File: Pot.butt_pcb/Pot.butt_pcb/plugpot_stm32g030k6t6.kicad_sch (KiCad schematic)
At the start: 7 parts, among them J1 Conn_01x05_Male, J2 Conn_01x06_Male, SW1 SW_Push, U1 STM32G030K6T6

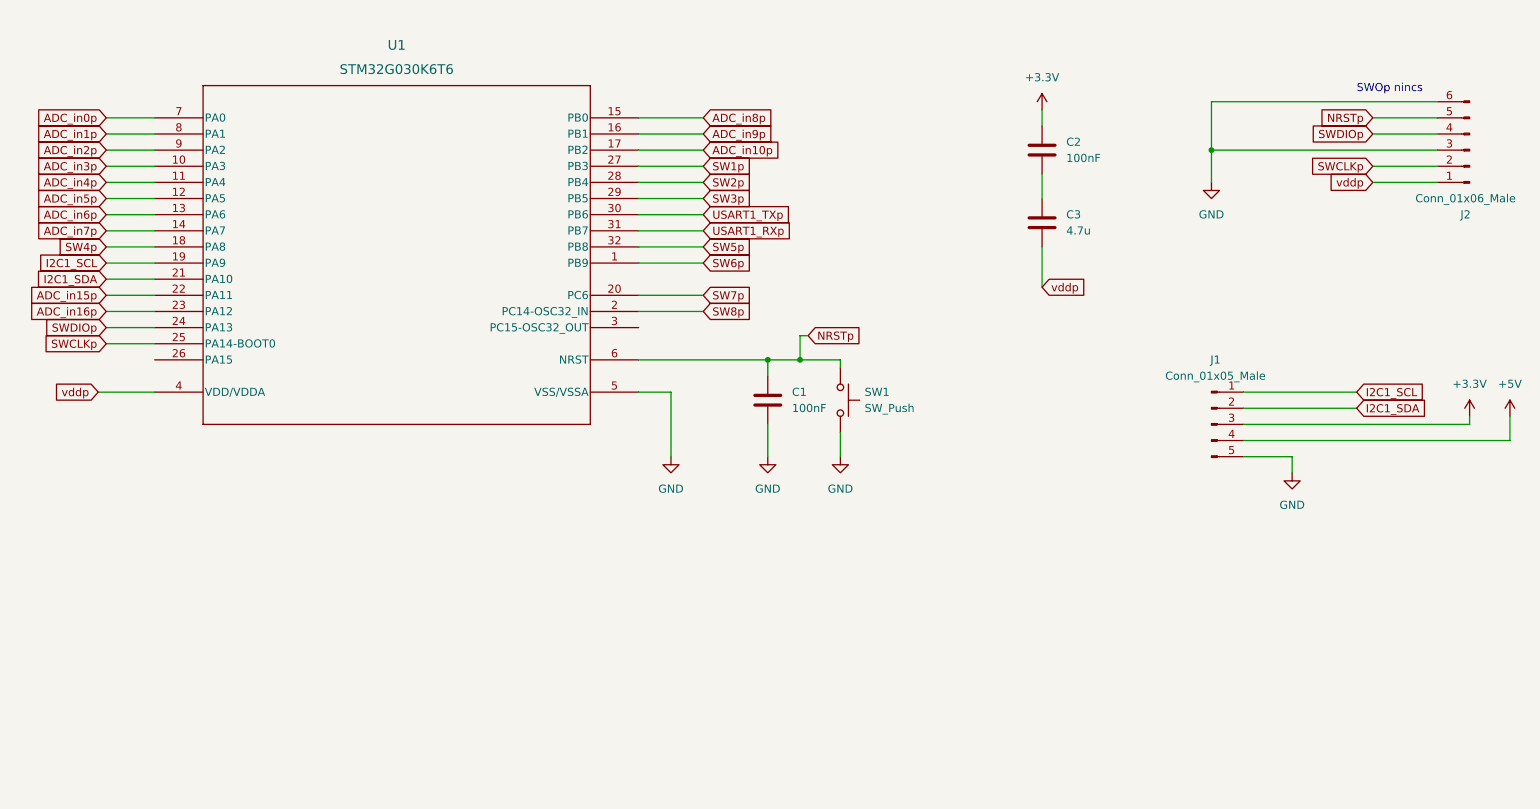
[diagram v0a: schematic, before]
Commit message: fixing keyboard and pot project schematics
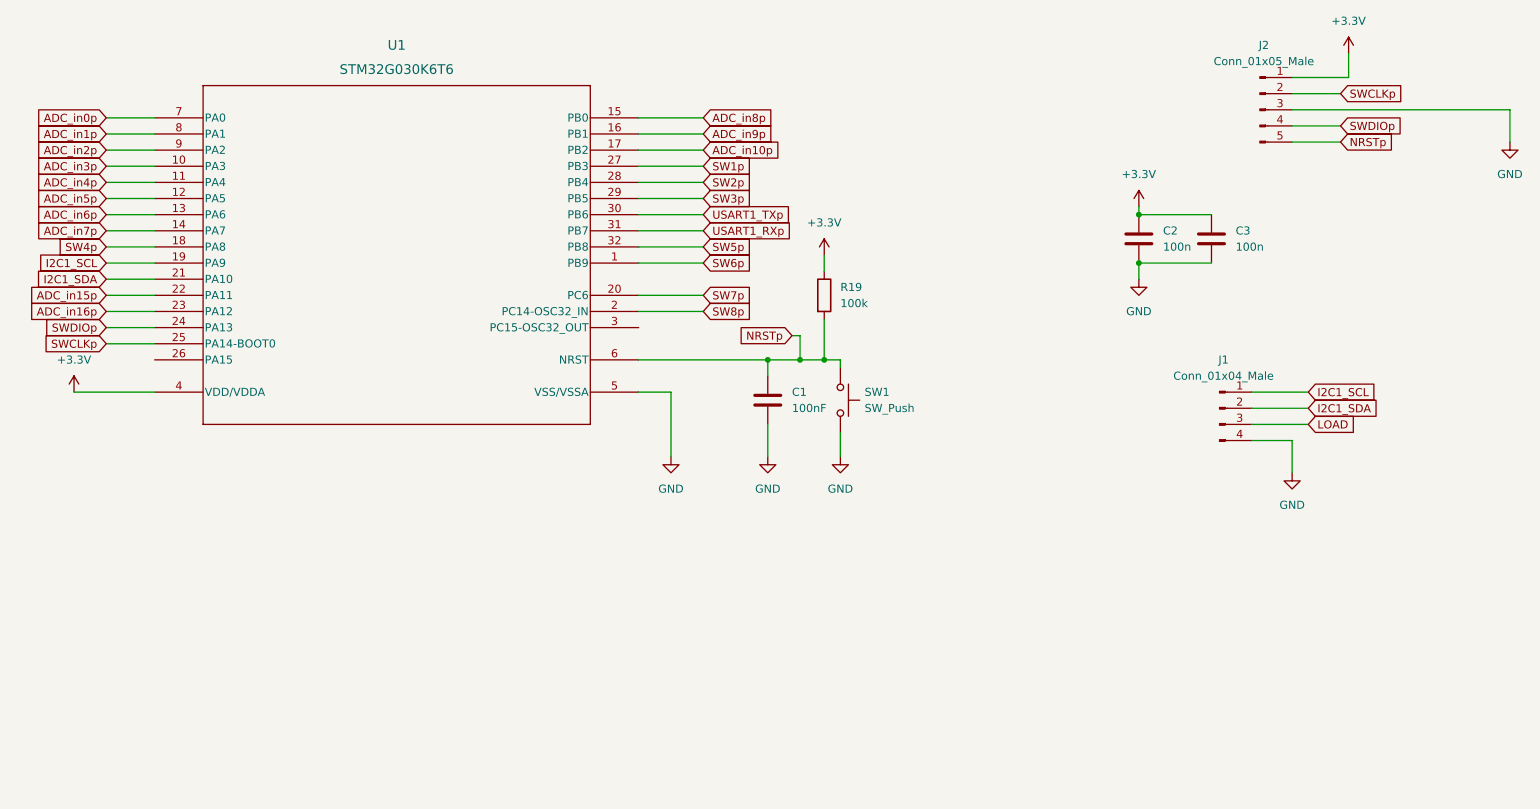
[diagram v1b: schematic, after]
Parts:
- removed J1: Conn_01x05_Male, symbol Connector:Conn_01x05_Male
- removed J2: Conn_01x06_Male, Connector_PinSocket_2.54mm:PinSocket_1x06_P2.54mm_Horizontal, symbol Connector:Conn_01x06_Male
- added J1: Conn_01x04_Male, symbol Connector:Conn_01x04_Male
- added J2: Conn_01x05_Male, symbol Connector:Conn_01x05_Male
- added R19: 100k, Resistor_SMD:R_0805_2012Metric_Pad1.20x1.40mm_HandSolder, symbol Device:R
- C2: value 100nF -> 100n
- C3: value 4.7u -> 100n
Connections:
- net +3V3: now also C3.1, U1.4 (VDD/VDDA), J2.1 (Pin_1), R19.1
- net GND: now also C2.2, C3.2, J1.4 (Pin_4), J2.3 (Pin_3)
- net I2C1_SCL: now also J1.1 (Pin_1)
- net I2C1_SDA: now also J1.2 (Pin_2)
- net NRSTp: now also J2.5 (Pin_5), R19.2
- net SWCLKp: now also J2.2 (Pin_2)
- net SWDIOp: now also J2.4 (Pin_4)
- removed net vddp: C3.2, U1.4 (VDD/VDDA)
- new net LOAD: J1.3 (Pin_3)
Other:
- note removed: "SWOp nincs"

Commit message: main_func pcb done
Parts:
- added D53: GREEN LED, LED_SMD:LED_0805_2012Metric_Pad1.15x1.40mm_HandSolder, symbol Device:LED
- added D54: RED LED, LED_SMD:LED_0805_2012Metric_Pad1.15x1.40mm_HandSolder, symbol Device:LED
- added R27, R28: 1k, Resistor_SMD:R_0805_2012Metric_Pad1.20x1.40mm_HandSolder, symbol Device:R
- C2, C3: value 100n -> 100nF
- J1: footprint (none) -> Connector_PinSocket_2.54mm:PinSocket_1x04_P2.54mm_Horizontal
- J2: footprint (none) -> Connector_PinSocket_2.54mm:PinSocket_1x05_P2.54mm_Horizontal
- SW1: footprint (none) -> tactile_button:ROCPU Switches TP10721645
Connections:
- net +3V3: now also D53.2 (A)
- net GND: now also D54.1 (K)
- net USART1_TXp: now also R27.1, R28.1
- new net: D54.2 (A), R28.2
- new net: D53.1 (K), R27.2
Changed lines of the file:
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@@
   (junction (at 147.32 88.9) (diameter 0) (color 0 0 0 0)
   )
+  (junction (at 191.3094 115.6909) (diameter 0) (color 0 0 0 0)
+  )
   (junction (at 205.74 66.04) (diameter 0) (color 0 0 0 0)
   )
@@
   (junction (at 156.21 88.9) (diameter 0) (color 0 0 0 0)
   )
+  (wire (pts (xy 173.5294 115.6909) (xy 173.5294 119.5009))
+    (stroke (width 0) (type default) (color 0 0 0 0))
+  )
   (wire (pts (xy 223.52 93.98) (xy 232.41 93.98))
     (stroke (width 0) (type default) (color 0 0 0 0))
@@
     (stroke (width 0) (type default) (color 0 0 0 0))
   )
+  (wire (pts (xy 191.3094 115.6909) (xy 191.3094 119.5009))
+    (stroke (width 0) (type default) (color 0 0 0 0))
+  )
   (wire (pts (xy 43.18 81.28) (xy 50.8 81.28))
     (stroke (width 0) (type default) (color 0 0 0 0))
@@
     (stroke (width 0) (type default) (color 0 0 0 0))
   )
+  (wire (pts (xy 173.5294 148.7109) (xy 173.5294 139.8209))
+    (stroke (width 0) (type default) (color 0 0 0 0))
+  )
   (wire (pts (xy 229.87 49.53) (xy 264.16 49.53))
     (stroke (width 0) (type default) (color 0 0 0 0))
@@
     (stroke (width 0) (type default) (color 0 0 0 0))
   )
+  (wire (pts (xy 198.9294 115.6909) (xy 191.3094 115.6909))
+    (stroke (width 0) (type default) (color 0 0 0 0))
+  )
   (wire (pts (xy 132.08 93.98) (xy 132.08 104.14))
     (stroke (width 0) (type default) (color 0 0 0 0))
@@
     (stroke (width 0) (type default) (color 0 0 0 0))
   )
+  (wire (pts (xy 191.3094 127.1209) (xy 191.3094 132.2009))
+    (stroke (width 0) (type default) (color 0 0 0 0))
+  )
   (wire (pts (xy 127 66.04) (xy 137.16 66.04))
     (stroke (width 0) (type default) (color 0 0 0 0))
@@
     (stroke (width 0) (type default) (color 0 0 0 0))
   )
+  (wire (pts (xy 168.4494 146.1709) (xy 168.4494 148.7109))
+    (stroke (width 0) (type default) (color 0 0 0 0))
+  )
+  (wire (pts (xy 191.3094 115.6909) (xy 173.5294 115.6909))
+    (stroke (width 0) (type default) (color 0 0 0 0))
+  )
   (wire (pts (xy 156.21 72.39) (xy 156.21 74.93))
     (stroke (width 0) (type default) (color 0 0 0 0))
@@
     (stroke (width 0) (type default) (color 0 0 0 0))
   )
+  (wire (pts (xy 173.5294 127.1209) (xy 173.5294 132.2009))
+    (stroke (width 0) (type default) (color 0 0 0 0))
+  )
   (wire (pts (xy 205.74 73.66) (xy 205.74 76.2))
     (stroke (width 0) (type default) (color 0 0 0 0))
   )
+  (wire (pts (xy 191.3094 139.8209) (xy 191.3094 147.4409))
+    (stroke (width 0) (type default) (color 0 0 0 0))
+  )
   (wire (pts (xy 127 73.66) (xy 137.16 73.66))
     (stroke (width 0) (type default) (color 0 0 0 0))
   )
+  (wire (pts (xy 168.4494 148.7109) (xy 173.5294 148.7109))
+    (stroke (width 0) (type default) (color 0 0 0 0))
+  )
   (wire (pts (xy 229.87 101.6) (xy 229.87 106.68))
     (stroke (width 0) (type default) (color 0 0 0 0))
@@
     (effects (font (size 1.27 1.27)) (justify left))
     (property "Intersheet References" "${INTERSHEET_REFS}" (id 0) (at 144.5926 71.0406 0)
+      (effects (font (size 1.27 1.27)) (justify left) hide)
+    )
+  )
+  (global_label "USART1_TXp" (shape input) (at 198.9294 115.6909 0) (fields_autoplaced)
+    (effects (font (size 1.27 1.27)) (justify left))
+    (property "Intersheet References" "${INTERSHEET_REFS}" (id 0) (at 212.712 115.6115 0)
       (effects (font (size 1.27 1.27)) (justify left) hide)
     )
@@
     (property "Reference" "J2" (id 0) (at 225.425 39.37 0))
     (property "Value" "Conn_01x05_Male" (id 1) (at 225.425 41.91 0))
-    (property "Footprint" "" (id 2) (at 224.79 49.53 0)
+    (property "Footprint" "Connector_PinSocket_2.54mm:PinSocket_1x05_P2.54mm_Horizontal" (id 2) (at 224.79 49.53 0)
       (effects (font (size 1.27 1.27)) hide)
     )
@@
       (effects (font (size 1.27 1.27)) (justify left))
     )
-    (property "Value" "100n" (id 1) (at 220.98 71.1199 0)
+    (property "Value" "100nF" (id 1) (at 220.98 71.1199 0)
       (effects (font (size 1.27 1.27)) (justify left))
     )
@@
     (property "Reference" "J1" (id 0) (at 219.075 88.9 0))
     (property "Value" "Conn_01x04_Male" (id 1) (at 219.075 91.44 0))
-    (property "Footprint" "" (id 2) (at 218.44 96.52 0)
+    (property "Footprint" "Connector_PinSocket_2.54mm:PinSocket_1x04_P2.54mm_Horizontal" (id 2) (at 218.44 96.52 0)
       (effects (font (size 1.27 1.27)) hide)
     )
@@
     (pin "1")
   )
+  (symbol (lib_id "power:+3.3V") (at 168.4494 146.1709 0) (unit 1)
+    (in_bom yes) (on_board yes) (fields_autoplaced)
+    (property "Reference" "#PWR022" (id 0) (at 168.4494 149.9809 0)
+      (effects (font (size 1.27 1.27)) hide)
+    )
+    (property "Value" "+3.3V" (id 1) (at 168.4494 141.0909 0))
+    (property "Footprint" "" (id 2) (at 168.4494 146.1709 0)
+      (effects (font (size 1.27 1.27)) hide)
+    )
+    (property "Datasheet" "" (id 3) (at 168.4494 146.1709 0)
+      (effects (font (size 1.27 1.27)) hide)
+    )
+    (pin "1")
+  )
   (symbol (lib_id "power:+3.3V") (at 205.74 64.77 0) (unit 1)
     (in_bom yes) (on_board yes) (fields_autoplaced)
@@
       (effects (font (size 1.27 1.27)) (justify left))
     )
-    (property "Footprint" "" (id 2) (at 163.83 95.25 0)
+    (property "Footprint" "tactile_button:ROCPU Switches TP10721645" (id 2) (at 163.83 95.25 0)
       (effects (font (size 1.27 1.27)) hide)
     )
     (property "Datasheet" "~" (id 3) (at 163.83 95.25 0)
+      (effects (font (size 1.27 1.27)) hide)
+    )
+    (pin "1")
+    (pin "2")
+  )
+  (symbol (lib_id "Device:R") (at 191.3094 123.3109 0) (unit 1)
+    (in_bom yes) (on_board yes) (fields_autoplaced)
+    (property "Reference" "R28" (id 0) (at 193.8494 122.0408 0)
+      (effects (font (size 1.27 1.27)) (justify left))
+    )
+    (property "Value" "1k" (id 1) (at 193.8494 124.5808 0)
+      (effects (font (size 1.27 1.27)) (justify left))
+    )
+    (property "Footprint" "Resistor_SMD:R_0805_2012Metric_Pad1.20x1.40mm_HandSolder" (id 2) (at 189.5314 123.3109 90)
+      (effects (font (size 1.27 1.27)) hide)
+    )
+    (property "Datasheet" "~" (id 3) (at 191.3094 123.3109 0)
       (effects (font (size 1.27 1.27)) hide)
     )
@@
     (pin "9")
   )
+  (symbol (lib_id "power:GND") (at 191.3094 147.4409 0) (unit 1)
+    (in_bom yes) (on_board yes) (fields_autoplaced)
+    (property "Reference" "#PWR023" (id 0) (at 191.3094 153.7909 0)
+      (effects (font (size 1.27 1.27)) hide)
+    )
+    (property "Value" "GND" (id 1) (at 191.3094 152.5209 0))
+    (property "Footprint" "" (id 2) (at 191.3094 147.4409 0)
+      (effects (font (size 1.27 1.27)) hide)
+    )
+    (property "Datasheet" "" (id 3) (at 191.3094 147.4409 0)
+      (effects (font (size 1.27 1.27)) hide)
+    )
+    (pin "1")
+  )
   (symbol (lib_id "Device:C") (at 205.74 69.85 0) (unit 1)
     (in_bom yes) (on_board yes) (fields_autoplaced)
@@
       (effects (font (size 1.27 1.27)) (justify left))
     )
-    (property "Value" "100n" (id 1) (at 209.55 71.1199 0)
+    (property "Value" "100nF" (id 1) (at 209.55 71.1199 0)
       (effects (font (size 1.27 1.27)) (justify left))
     )
@@
     (pin "1")
   )
+  (symbol (lib_id "Device:LED") (at 191.3094 136.0109 90) (unit 1)
+    (in_bom yes) (on_board yes) (fields_autoplaced)
+    (property "Reference" "D54" (id 0) (at 195.1194 136.3283 90)
+      (effects (font (size 1.27 1.27)) (justify right))
+    )
+    (property "Value" "RED LED" (id 1) (at 195.1194 138.8683 90)
+      (effects (font (size 1.27 1.27)) (justify right))
+    )
+    (property "Footprint" "LED_SMD:LED_0805_2012Metric_Pad1.15x1.40mm_HandSolder" (id 2) (at 191.3094 136.0109 0)
+      (effects (font (size 1.27 1.27)) hide)
+    )
+    (property "Datasheet" "~" (id 3) (at 191.3094 136.0109 0)
+      (effects (font (size 1.27 1.27)) hide)
+    )
+    (pin "1")
+    (pin "2")
+  )
   (symbol (lib_id "power:GND") (at 132.08 104.14 0) (unit 1)
     (in_bom yes) (on_board yes) (fields_autoplaced)
@@
     (pin "1")
   )
+  (symbol (lib_id "Device:R") (at 173.5294 123.3109 0) (unit 1)
+    (in_bom yes) (on_board yes) (fields_autoplaced)
+    (property "Reference" "R27" (id 0) (at 176.0694 122.0408 0)
+      (effects (font (size 1.27 1.27)) (justify left))
+    )
+    (property "Value" "1k" (id 1) (at 176.0694 124.5808 0)
+      (effects (font (size 1.27 1.27)) (justify left))
+    )
+    (property "Footprint" "Resistor_SMD:R_0805_2012Metric_Pad1.20x1.40mm_HandSolder" (id 2) (at 171.7514 123.3109 90)
+      (effects (font (size 1.27 1.27)) hide)
+    )
+    (property "Datasheet" "~" (id 3) (at 173.5294 123.3109 0)
+      (effects (font (size 1.27 1.27)) hide)
+    )
+    (pin "1")
+    (pin "2")
+  )
+  (symbol (lib_id "Device:LED") (at 173.5294 136.0109 270) (unit 1)
+    (in_bom yes) (on_board yes) (fields_autoplaced)
+    (property "Reference" "D53" (id 0) (at 176.0694 133.1533 90)
+      (effects (font (size 1.27 1.27)) (justify left))
+    )
+    (property "Value" "GREEN LED" (id 1) (at 176.0694 135.6933 90)
+      (effects (font (size 1.27 1.27)) (justify left))
+    )
+    (property "Footprint" "LED_SMD:LED_0805_2012Metric_Pad1.15x1.40mm_HandSolder" (id 2) (at 173.5294 136.0109 0)
+      (effects (font (size 1.27 1.27)) hide)
+    )
+    (property "Datasheet" "~" (id 3) (at 173.5294 136.0109 0)
+      (effects (font (size 1.27 1.27)) hide)
+    )
+    (pin "1")
+    (pin "2")
+  )
 )

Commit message: Pot.but_pcb in progress
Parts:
- J1: footprint Connector_PinSocket_2.54mm:PinSocket_1x04_P2.54mm_Horizontal -> Connector_PinSocket_2.54mm:PinSocket_1x04_P2.54mm_Vertical
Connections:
- net SW1p: now also U1.18 (PA8); no longer U1.27 (PB3)
- net SW2p: now also U1.20 (PC6); no longer U1.28 (PB4)
- net SW3p: now also U1.27 (PB3); no longer U1.29 (PB5)
- net SW4p: now also U1.28 (PB4); no longer U1.18 (PA8)
- net SW5p: now also U1.29 (PB5); no longer U1.32 (PB8)
- net SW6p: now also U1.32 (PB8); no longer U1.1 (PB9)
- net SW7p: now also U1.2 (PC14-OSC32_IN); no longer U1.20 (PC6)
- net SW8p: now also U1.1 (PB9); no longer U1.2 (PC14-OSC32_IN)
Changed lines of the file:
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@@
     )
   )
-  (global_label "SW2p" (shape input) (at 137.16 60.96 0) (fields_autoplaced)
+  (global_label "SW4p" (shape input) (at 137.16 60.96 0) (fields_autoplaced)
     (effects (font (size 1.27 1.27)) (justify left))
     (property "Intersheet References" "${INTERSHEET_REFS}" (id 0) (at 144.5926 60.8806 0)
@@
     )
   )
-  (global_label "SW3p" (shape input) (at 137.16 63.5 0) (fields_autoplaced)
+  (global_label "SW5p" (shape input) (at 137.16 63.5 0) (fields_autoplaced)
     (effects (font (size 1.27 1.27)) (justify left))
     (property "Intersheet References" "${INTERSHEET_REFS}" (id 0) (at 144.5926 63.4206 0)
@@
     )
   )
-  (global_label "SW5p" (shape input) (at 137.16 71.12 0) (fields_autoplaced)
+  (global_label "SW6p" (shape input) (at 137.16 71.12 0) (fields_autoplaced)
     (effects (font (size 1.27 1.27)) (justify left))
     (property "Intersheet References" "${INTERSHEET_REFS}" (id 0) (at 144.5926 71.0406 0)
@@
     )
   )
-  (global_label "SW1p" (shape input) (at 137.16 58.42 0) (fields_autoplaced)
+  (global_label "SW3p" (shape input) (at 137.16 58.42 0) (fields_autoplaced)
     (effects (font (size 1.27 1.27)) (justify left))
     (property "Intersheet References" "${INTERSHEET_REFS}" (id 0) (at 144.5926 58.3406 0)
@@
     )
   )
-  (global_label "SW4p" (shape input) (at 43.18 71.12 180) (fields_autoplaced)
+  (global_label "SW1p" (shape input) (at 43.18 71.12 180) (fields_autoplaced)
     (effects (font (size 1.27 1.27)) (justify right))
     (property "Intersheet References" "${INTERSHEET_REFS}" (id 0) (at 35.7474 71.0406 0)
@@
     )
   )
-  (global_label "SW8p" (shape input) (at 137.16 81.28 0) (fields_autoplaced)
+  (global_label "SW7p" (shape input) (at 137.16 81.28 0) (fields_autoplaced)
     (effects (font (size 1.27 1.27)) (justify left))
     (property "Intersheet References" "${INTERSHEET_REFS}" (id 0) (at 144.5926 81.2006 0)
@@
     )
   )
-  (global_label "SW7p" (shape input) (at 137.16 78.74 0) (fields_autoplaced)
+  (global_label "SW2p" (shape input) (at 137.16 78.74 0) (fields_autoplaced)
     (effects (font (size 1.27 1.27)) (justify left))
     (property "Intersheet References" "${INTERSHEET_REFS}" (id 0) (at 144.5926 78.6606 0)
@@
     )
   )
-  (global_label "SW6p" (shape input) (at 137.16 73.66 0) (fields_autoplaced)
+  (global_label "SW8p" (shape input) (at 137.16 73.66 0) (fields_autoplaced)
     (effects (font (size 1.27 1.27)) (justify left))
     (property "Intersheet References" "${INTERSHEET_REFS}" (id 0) (at 144.5926 73.5806 0)
@@
     (property "Reference" "J1" (id 0) (at 219.075 88.9 0))
     (property "Value" "Conn_01x04_Male" (id 1) (at 219.075 91.44 0))
-    (property "Footprint" "Connector_PinSocket_2.54mm:PinSocket_1x04_P2.54mm_Horizontal" (id 2) (at 218.44 96.52 0)
-      (effects (font (size 1.27 1.27)) hide)
-    )
+    (property "Footprint" "Connector_PinSocket_2.54mm:PinSocket_1x04_P2.54mm_Vertical" (id 2) (at 218.44 96.52 0)
+      (effects (font (size 1.27 1.27)) hide)
+    )

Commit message: pcb design fixing
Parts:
- removed C3: 100nF, Capacitor_SMD:C_0805_2012Metric_Pad1.18x1.45mm_HandSolder, symbol Device:C
- removed J1: Conn_01x04_Male, Connector_PinSocket_2.54mm:PinSocket_1x04_P2.54mm_Vertical, symbol Connector:Conn_01x04_Male
- removed R27, R28: 1k, Resistor_SMD:R_0805_2012Metric_Pad1.20x1.40mm_HandSolder, symbol Device:R
- added J1: Conn_01x10_Male, Connector_IDC:IDC-Header_2x05_P2.54mm_Horizontal, symbol Connector:Conn_01x10_Male
- added R1, R2: 1k, Resistor_SMD:R_0805_2012Metric_Pad1.20x1.40mm_HandSolder, symbol Device:R
- D53: value GREEN LED -> RED LED
- D54: value RED LED -> GREEN LED
- R19: value 100k -> 10k
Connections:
- net USART1_RXp is gone; now on net SW7p: U1.31 (PB7)
- net USART1_TXp is gone; now on net SW6p: U1.30 (PB6)
- net +3V3: no longer D53.2 (A)
- net GND: now also D53.1 (K), J1.10 (Pin_10), J1.2 (Pin_2), J1.4 (Pin_4), J1.6 (Pin_6), J1.8 (Pin_8), J1.9 (Pin_9)
- net I2C1_SCL: now also J1.7 (Pin_7)
- net I2C1_SDA: now also J1.5 (Pin_5)
- net LOAD: now also J1.1 (Pin_1), J1.3 (Pin_3), R2.1
- net SW6p: no longer U1.32 (PB8)
- net SW7p: no longer U1.2 (PC14-OSC32_IN)
- net SW8p: now also U1.32 (PB8); no longer U1.1 (PB9)
- net at D54.2 (A): now also R2.2
- net ADC_in15p renamed ADC_in11p
- new net: D53.2 (A), R1.2
- new net STATUS_LEDp: R1.1, U1.1 (PB9)
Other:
- moved on the sheet: C2
